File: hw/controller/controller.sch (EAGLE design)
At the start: 86 parts, among them J1 JST-PH3SMT_VERT, J2 JST-PH3SMT_VERT, Q1 TPN1R603PL, Q2 TPN1R603PL, Q3 TPN1R603PL, Q4 TPN1R603PL, Q5 TPN1R603PL, Q6 TPN1R603PL, U1 STM32F4R_64PIN, U2 DRV8323RS, U3 AS5147, U4 MAX13431E, U5 MAX13433EETD+T, X1 8.0MHz

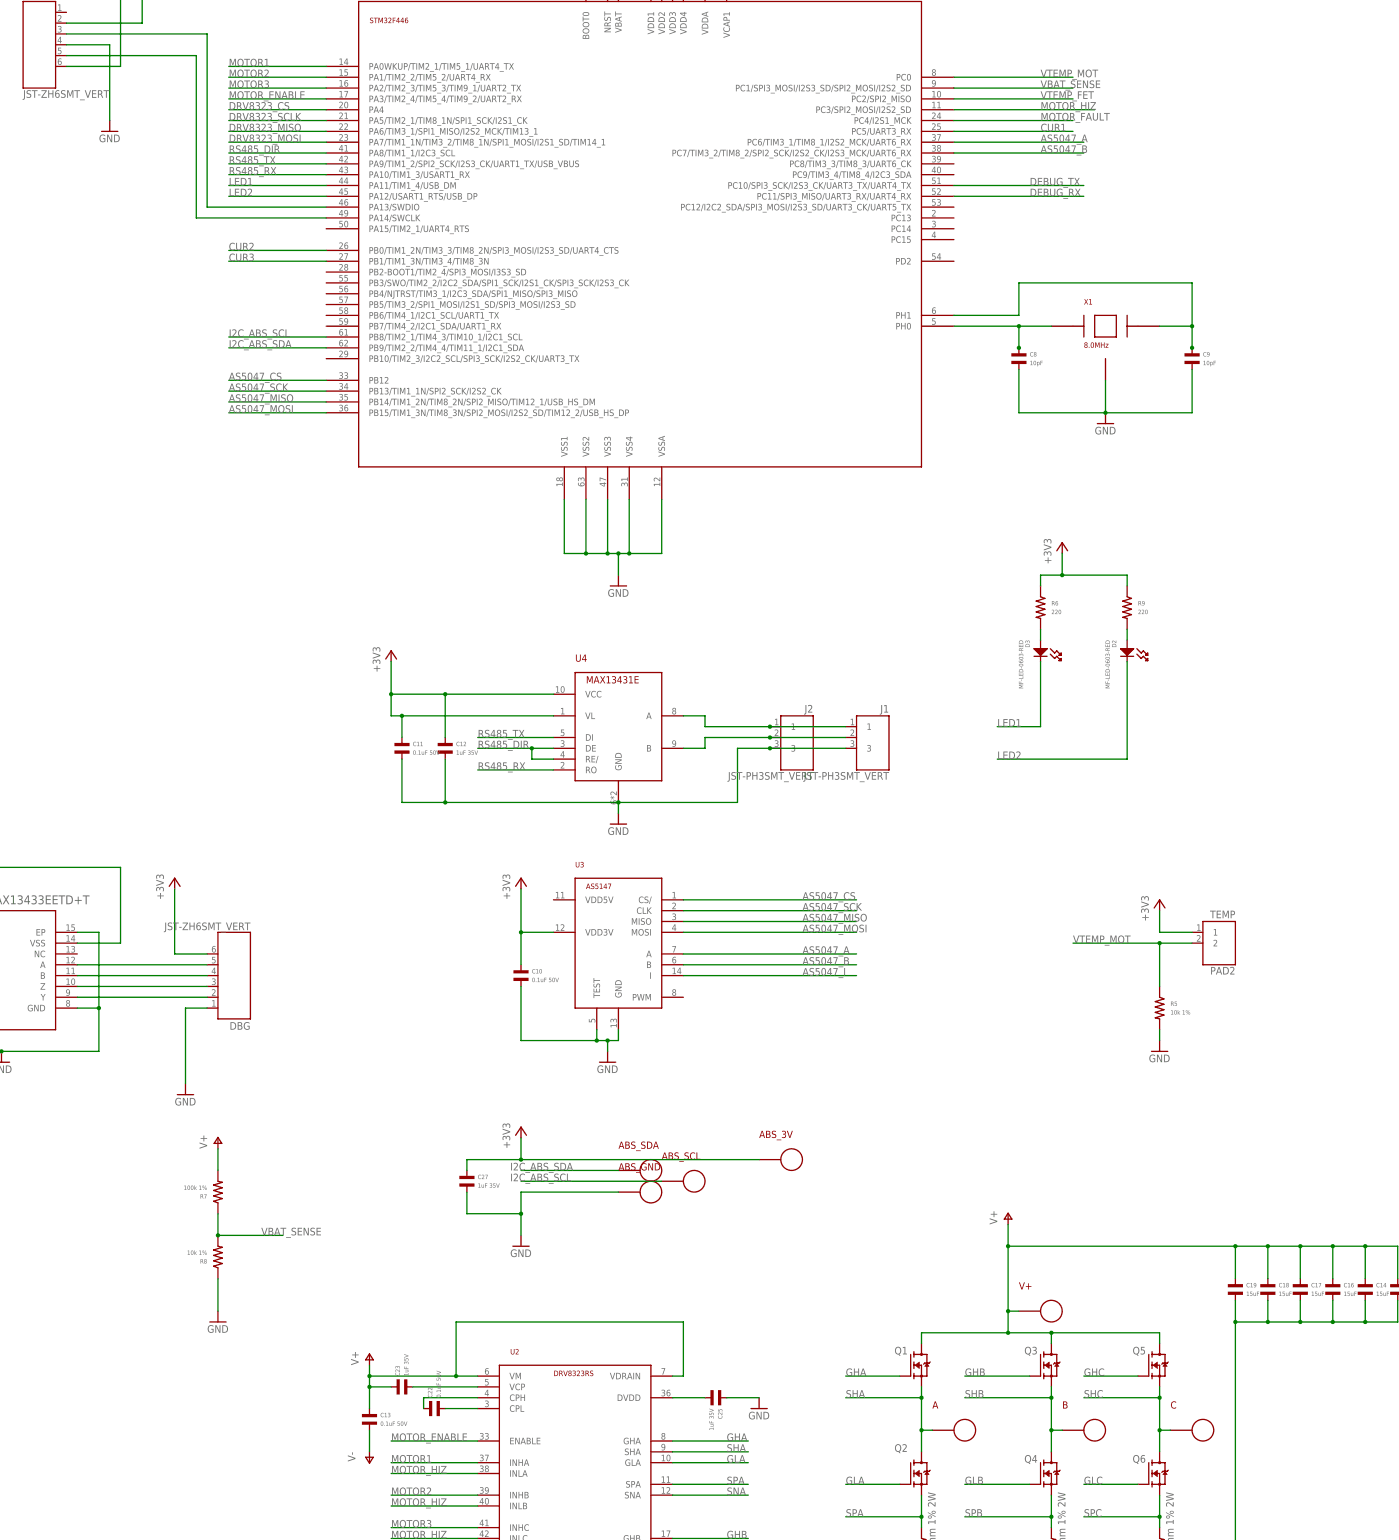
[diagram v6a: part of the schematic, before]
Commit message: Fix more errata in controller board
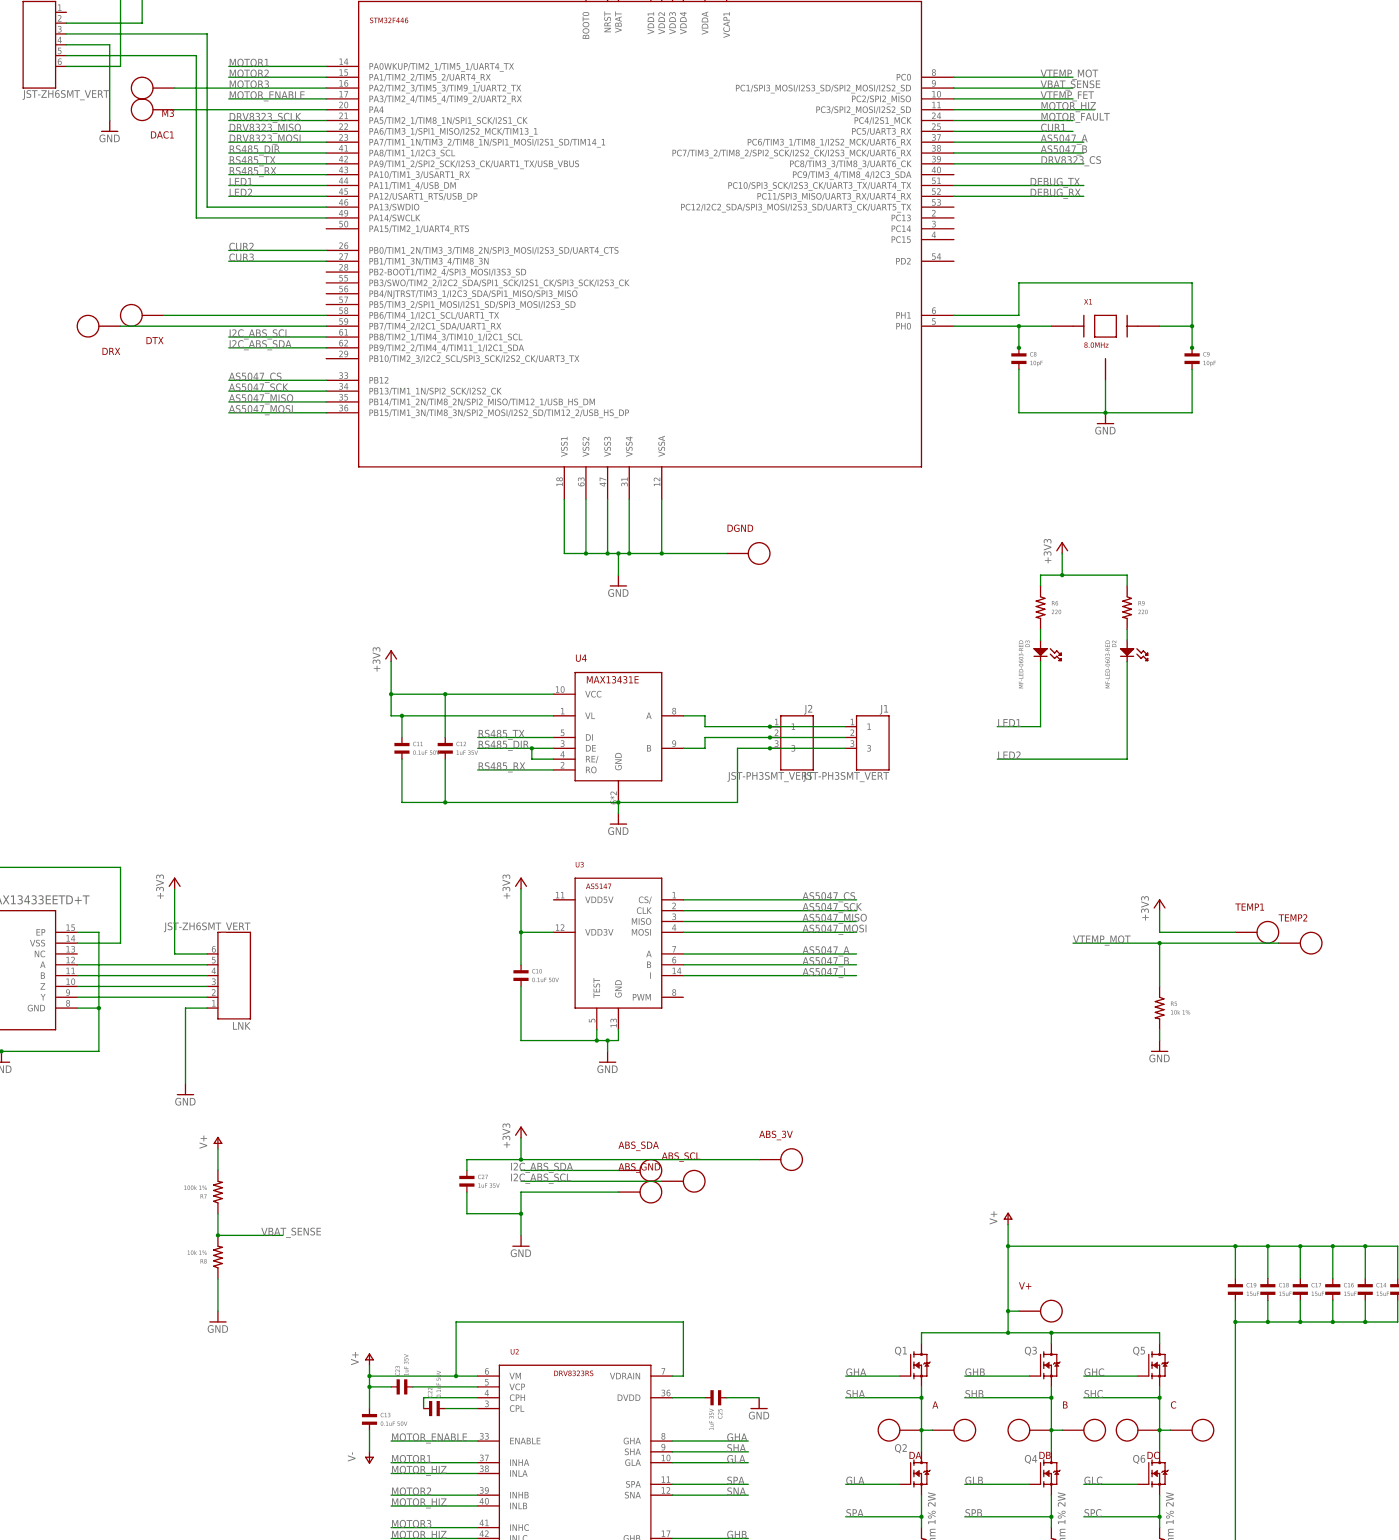
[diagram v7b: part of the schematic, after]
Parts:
- removed TEMP: PAD2, controller:PAD2
- added DA, DAC1, DB, DC, DGND, DRX, DTX, M3, TEMP1, TEMP2: PAD24AWG_PAD, controller:PAD24AWG_PAD
- R1: device mfpassives:RESISTOR_0402 -> mfpassives:RESISTOR_0603; MPN MF-RES-0402-220 -> MF-RES-0603-220
- renumbered DBG to LNK
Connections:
- new net N$1: DAC1.P$1, U1.PA4
- new net N$2: DTX.P$1, U1.PB6/TIM4_1/I2C1_SCL/UART1_TX
- new net N$3: DRX.P$1, U1.PB7/TIM4_2/I2C1_SDA/UART1_RX
- net +3V3: now also TEMP1.P$1; no longer TEMP.1
- net DRV8323_CS: now also U1.PC8/TIM3_3/TIM8_3/UART6_CK; no longer U1.PA4
- net GND: now also DGND.P$1
- net MOTOR3: now also M3.P$1
- net SHA: now also DA.P$1
- net SHB: now also DB.P$1
- net SHC: now also DC.P$1
- net VTEMP_MOT: now also TEMP2.P$1; no longer TEMP.2
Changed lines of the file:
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@@
 <part name="GND16" library="supply1" deviceset="GND" device=""/>
 <part name="+3V8" library="supply1" deviceset="+3V3" device=""/>
-<part name="R1" library="mfpassives" deviceset="RESISTOR" device="_0402" value="220">
+<part name="R1" library="mfpassives" deviceset="RESISTOR" device="_0603" value="220">
 <attribute name="HOUSEPART" value="1"/>
-<attribute name="MPN" value="MF-RES-0402-220"/>
+<attribute name="MPN" value="MF-RES-0603-220"/>
 </part>
 <part name="C2" library="mfpassives" deviceset="CAPACITOR_NP" device="_0402" value="0.1uF 50V">
@@
 <part name="GND10" library="supply1" deviceset="GND" device=""/>
 <part name="+3V5" library="supply1" deviceset="+3V3" device=""/>
-<part name="TEMP" library="controller" deviceset="PAD2" device="">
-<attribute name="POPULATE" value="0"/>
-</part>
 <part name="+3V6" library="supply1" deviceset="+3V3" device=""/>
 <part name="GND11" library="supply1" deviceset="GND" device=""/>
@@
 <part name="+3V11" library="supply1" deviceset="+3V3" device=""/>
 <part name="GND13" library="supply1" deviceset="GND" device=""/>
-<part name="DBG" library="controller" deviceset="JST-ZH6" device="SMT_VERT" value="JST-ZH6SMT_VERT">
+<part name="LNK" library="controller" deviceset="JST-ZH6" device="SMT_VERT" value="JST-ZH6SMT_VERT">
 <attribute name="MF" value="JST"/>
 <attribute name="MPN" value="B6B-ZR-SM4-TF(LF)(SN)"/>
@@
 <attribute name="MPN" value="C1005X7R1H104K050BE"/>
 </part>
+<part name="DAC1" library="controller" deviceset="PAD" device="24AWG_PAD"/>
+<part name="M3" library="controller" deviceset="PAD" device="24AWG_PAD"/>
+<part name="DTX" library="controller" deviceset="PAD" device="24AWG_PAD"/>
+<part name="DRX" library="controller" deviceset="PAD" device="24AWG_PAD"/>
+<part name="TEMP1" library="controller" deviceset="PAD" device="24AWG_PAD"/>
+<part name="TEMP2" library="controller" deviceset="PAD" device="24AWG_PAD"/>
+<part name="DGND" library="controller" deviceset="PAD" device="24AWG_PAD"/>
+<part name="DA" library="controller" deviceset="PAD" device="24AWG_PAD"/>
+<part name="DB" library="controller" deviceset="PAD" device="24AWG_PAD"/>
+<part name="DC" library="controller" deviceset="PAD" device="24AWG_PAD"/>
 </parts>
 <sheets>
@@
 <instance part="GND10" gate="1" x="66.04" y="-200.66"/>
 <instance part="+3V5" gate="G$1" x="66.04" y="-172.72"/>
-<instance part="TEMP" gate="A" x="228.6" y="-129.54" rot="MR0">
-<attribute name="POPULATE" x="228.6" y="-129.54" size="1.778" layer="96" rot="MR0" display="off"/>
-</instance>
 <instance part="+3V6" gate="G$1" x="215.9" y="-119.38"/>
 <instance part="GND11" gate="1" x="215.9" y="-154.94"/>
@@
 <instance part="+3V11" gate="G$1" x="-93.98" y="-104.14"/>
 <instance part="GND13" gate="1" x="-55.88" y="-157.48"/>
-<instance part="DBG" gate="A" x="-2.54" y="-137.16" rot="R180">
+<instance part="LNK" gate="A" x="-2.54" y="-137.16" rot="R180">
 <attribute name="POPULATE" x="-2.54" y="-137.16" size="1.778" layer="96" rot="R180" display="off"/>
 <attribute name="MPN" x="-2.54" y="-137.16" size="1.778" layer="96" rot="R180" display="off"/>
@@
 <attribute name="MF" x="228.6" y="-320.04" size="1.778" layer="96" display="off"/>
 </instance>
+<instance part="DAC1" gate="G$1" x="-22.86" y="66.04" rot="R180"/>
+<instance part="M3" gate="G$1" x="-22.86" y="71.12" rot="R180"/>
+<instance part="DTX" gate="G$1" x="-25.4" y="17.78" rot="R180"/>
+<instance part="DRX" gate="G$1" x="-35.56" y="15.24" rot="R180"/>
+<instance part="TEMP1" gate="G$1" x="241.3" y="-127"/>
+<instance part="TEMP2" gate="G$1" x="251.46" y="-129.54"/>
+<instance part="DGND" gate="G$1" x="121.92" y="-38.1"/>
+<instance part="DA" gate="G$1" x="152.4" y="-243.84" rot="R180"/>
+<instance part="DB" gate="G$1" x="182.88" y="-243.84" rot="R180"/>
+<instance part="DC" gate="G$1" x="208.28" y="-243.84" rot="R180"/>
 </instances>
 <busses>
@@
 <pinref part="+3V6" gate="G$1" pin="+3V3"/>
 <wire x1="215.9" y1="-121.92" x2="215.9" y2="-127" width="0.1524" layer="91"/>
-<pinref part="TEMP" gate="A" pin="1"/>
-<wire x1="215.9" y1="-127" x2="223.52" y2="-127" width="0.1524" layer="91"/>
+<pinref part="TEMP1" gate="G$1" pin="P$1"/>
+<wire x1="215.9" y1="-127" x2="233.68" y2="-127" width="0.1524" layer="91"/>
 </segment>
 <segment>
@@
 <pinref part="+3V10" gate="G$1" pin="+3V3"/>
 <wire x1="-15.24" y1="-116.84" x2="-15.24" y2="-132.08" width="0.1524" layer="91"/>
-<pinref part="DBG" gate="A" pin="6"/>
+<pinref part="LNK" gate="A" pin="6"/>
 <wire x1="-15.24" y1="-132.08" x2="-7.62" y2="-132.08" width="0.1524" layer="91"/>
 </segment>
@@
 <pinref part="U1" gate="G$1" pin="VSS4"/>
 <pinref part="U1" gate="G$1" pin="VSSA"/>
+<pinref part="DGND" gate="G$1" pin="P$1"/>
+<wire x1="99.06" y1="-38.1" x2="114.3" y2="-38.1" width="0.1524" layer="91"/>
+<junction x="99.06" y="-38.1"/>
 </segment>
 <segment>
@@
 <pinref part="GND3" gate="1" pin="GND"/>
 <wire x1="-12.7" y1="-162.56" x2="-12.7" y2="-144.78" width="0.1524" layer="91"/>
-<pinref part="DBG" gate="A" pin="1"/>
+<pinref part="LNK" gate="A" pin="1"/>
 <wire x1="-12.7" y1="-144.78" x2="-7.62" y2="-144.78" width="0.1524" layer="91"/>
 </segment>
@@
 <segment>
 <pinref part="U1" gate="G$1" pin="PA2/TIM2_3/TIM5_3/TIM9_1/UART2_TX"/>
-<wire x1="20.32" y1="71.12" x2="-2.54" y2="71.12" width="0.1524" layer="91"/>
+<wire x1="20.32" y1="71.12" x2="-15.24" y2="71.12" width="0.1524" layer="91"/>
 <label x="-2.54" y="71.12" size="1.778" layer="95"/>
+<pinref part="M3" gate="G$1" pin="P$1"/>
 </segment>
 </net>
@@
 </segment>
 <segment>
-<pinref part="U1" gate="G$1" pin="PA4"/>
-<wire x1="20.32" y1="66.04" x2="-2.54" y2="66.04" width="0.1524" layer="91"/>
-<label x="-2.54" y="66.04" size="1.778" layer="95"/>
+<pinref part="U1" gate="G$1" pin="PC8/TIM3_3/TIM8_3/UART6_CK"/>
+<wire x1="167.64" y1="53.34" x2="198.12" y2="53.34" width="0.1524" layer="91"/>
+<label x="187.96" y="53.34" size="1.778" layer="95"/>
 </segment>
 </net>
@@
 <wire x1="162.56" y1="-243.84" x2="160.02" y2="-243.84" width="0.1524" layer="91"/>
 <junction x="160.02" y="-243.84"/>
+<pinref part="DA" gate="G$1" pin="P$1"/>
 </segment>
 <segment>
@@
 <wire x1="193.04" y1="-243.84" x2="190.5" y2="-243.84" width="0.1524" layer="91"/>
 <junction x="190.5" y="-243.84"/>
+<pinref part="DB" gate="G$1" pin="P$1"/>
 </segment>
 <segment>
@@
 <wire x1="218.44" y1="-243.84" x2="215.9" y2="-243.84" width="0.1524" layer="91"/>
 <junction x="215.9" y="-243.84"/>
+<pinref part="DC" gate="G$1" pin="P$1"/>
 </segment>
 <segment>
@@
 <segment>
 <pinref part="U5" gate="A" pin="Y"/>
-<pinref part="DBG" gate="A" pin="2"/>
+<pinref part="LNK" gate="A" pin="2"/>
 <wire x1="-38.1" y1="-142.24" x2="-7.62" y2="-142.24" width="0.1524" layer="91"/>
 </segment>
@@
 <segment>
 <pinref part="U5" gate="A" pin="Z"/>
-<pinref part="DBG" gate="A" pin="3"/>
+<pinref part="LNK" gate="A" pin="3"/>
 <wire x1="-38.1" y1="-139.7" x2="-7.62" y2="-139.7" width="0.1524" layer="91"/>
 </segment>
@@
 <segment>
 <pinref part="U5" gate="A" pin="B"/>
-<pinref part="DBG" gate="A" pin="4"/>
+<pinref part="LNK" gate="A" pin="4"/>
 <wire x1="-38.1" y1="-137.16" x2="-7.62" y2="-137.16" width="0.1524" layer="91"/>
 </segment>
@@
 <segment>
 <pinref part="U5" gate="A" pin="A"/>
-<pinref part="DBG" gate="A" pin="5"/>
+<pinref part="LNK" gate="A" pin="5"/>
 <wire x1="-38.1" y1="-134.62" x2="-7.62" y2="-134.62" width="0.1524" layer="91"/>
 </segment>
@@
 <pinref part="R5" gate="G$1" pin="P$1"/>
 <wire x1="215.9" y1="-139.7" x2="215.9" y2="-129.54" width="0.1524" layer="91"/>
-<pinref part="TEMP" gate="A" pin="2"/>
-<wire x1="215.9" y1="-129.54" x2="223.52" y2="-129.54" width="0.1524" layer="91"/>
 <wire x1="215.9" y1="-129.54" x2="195.58" y2="-129.54" width="0.1524" layer="91"/>
 <junction x="215.9" y="-129.54"/>
 <label x="195.58" y="-129.54" size="1.778" layer="95"/>
+<pinref part="TEMP2" gate="G$1" pin="P$1"/>
+<wire x1="215.9" y1="-129.54" x2="243.84" y2="-129.54" width="0.1524" layer="91"/>
 </segment>
 <segment>
@@
 </segment>
 </net>
+<net name="N$1" class="0">
+<segment>
+<pinref part="DAC1" gate="G$1" pin="P$1"/>
+<pinref part="U1" gate="G$1" pin="PA4"/>
+<wire x1="-15.24" y1="66.04" x2="20.32" y2="66.04" width="0.1524" layer="91"/>
+</segment>
+</net>
+<net name="N$2" class="0">
+<segment>
+<pinref part="DTX" gate="G$1" pin="P$1"/>
+<pinref part="U1" gate="G$1" pin="PB6/TIM4_1/I2C1_SCL/UART1_TX"/>
+<wire x1="-17.78" y1="17.78" x2="20.32" y2="17.78" width="0.1524" layer="91"/>
+</segment>
+</net>
+<net name="N$3" class="0">
+<segment>
+<pinref part="DRX" gate="G$1" pin="P$1"/>
+<pinref part="U1" gate="G$1" pin="PB7/TIM4_2/I2C1_SDA/UART1_RX"/>
+<wire x1="-27.94" y1="15.24" x2="20.32" y2="15.24" width="0.1524" layer="91"/>
+</segment>
+</net>

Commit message: More tweaks to controller board
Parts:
- removed R10, R3: 100k 1%, mfpassives:RESISTOR_0402
- R11: value 100k 1% -> 33k 1%; MPN ERJ-2RKF1003X -> ERJ-2RKF3302X
- U5: MF (none) -> Maxim; MPN (none) -> MAX13433EETD+T; POPULATE (none) -> 1
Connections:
- net +3V3: no longer R10.P$1, R3.P$1
- net N$8: no longer R10.P$2, R3.P$2
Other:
- note removed: "3x 100k = 33.3k (to save part count)"
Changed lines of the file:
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@@
 <attribute name="MPN" value="C3216X5R1V156M160AC"/>
 </part>
-<part name="R3" library="mfpassives" deviceset="RESISTOR" device="_0402" value="100k 1%">
+<part name="R11" library="mfpassives" deviceset="RESISTOR" device="_0402" value="33k 1%">
 <attribute name="MF" value="Panasonic"/>
-<attribute name="MPN" value="ERJ-2RKF1003X"/>
-</part>
-<part name="R10" library="mfpassives" deviceset="RESISTOR" device="_0402" value="100k 1%">
-<attribute name="MF" value="Panasonic"/>
-<attribute name="MPN" value="ERJ-2RKF1003X"/>
-</part>
-<part name="R11" library="mfpassives" deviceset="RESISTOR" device="_0402" value="100k 1%">
-<attribute name="MF" value="Panasonic"/>
-<attribute name="MPN" value="ERJ-2RKF1003X"/>
+<attribute name="MPN" value="ERJ-2RKF3302X"/>
 </part>
 <part name="C29" library="mfpassives" deviceset="CAPACITOR_NP" device="_0402" value="1uF 35V">
@@
 <part name="ABS_SCL" library="controller" deviceset="PAD" device="24AWG_PAD"/>
 <part name="ABS_GND" library="controller" deviceset="PAD" device="24AWG_PAD"/>
-<part name="U5" library="controller" deviceset="MAX13433EETD+T" device=""/>
+<part name="U5" library="controller" deviceset="MAX13433EETD+T" device="">
+<attribute name="MF" value="Maxim"/>
+<attribute name="MPN" value="MAX13433EETD+T"/>
+<attribute name="POPULATE" value="1"/>
+</part>
 <part name="+3V11" library="supply1" deviceset="+3V3" device=""/>
 <part name="GND13" library="supply1" deviceset="GND" device=""/>
@@
 <sheet>
 <plain>
-<text x="145.034" y="-324.358" size="1.778" layer="91">3x 100k = 33.3k
-(to save part count)</text>
 </plain>
 <instances>
@@
 <attribute name="MF" x="233.68" y="-210.82" size="1.778" layer="96" display="off"/>
 </instance>
-<instance part="R3" gate="G$1" x="152.4" y="-330.2">
-<attribute name="MPN" x="152.4" y="-330.2" size="1.778" layer="96" display="off"/>
-<attribute name="MF" x="152.4" y="-330.2" size="1.778" layer="96" display="off"/>
-</instance>
-<instance part="R10" gate="G$1" x="144.78" y="-330.2">
-<attribute name="MPN" x="144.78" y="-330.2" size="1.778" layer="96" display="off"/>
-<attribute name="MF" x="144.78" y="-330.2" size="1.778" layer="96" display="off"/>
-</instance>
 <instance part="R11" gate="G$1" x="134.62" y="-330.2">
 <attribute name="MPN" x="134.62" y="-330.2" size="1.778" layer="96" display="off"/>
@@
 <instance part="ABS_SCL" gate="G$1" x="106.68" y="-185.42"/>
 <instance part="ABS_GND" gate="G$1" x="96.52" y="-187.96"/>
-<instance part="U5" gate="A" x="-76.2" y="-127"/>
+<instance part="U5" gate="A" x="-76.2" y="-127">
+<attribute name="MPN" x="-76.2" y="-127" size="1.778" layer="96" display="off"/>
+<attribute name="MF" x="-76.2" y="-127" size="1.778" layer="96" display="off"/>
+<attribute name="POPULATE" x="-76.2" y="-127" size="1.778" layer="96" display="off"/>
+</instance>
 <instance part="+3V11" gate="G$1" x="-93.98" y="-104.14"/>
 <instance part="GND13" gate="1" x="-55.88" y="-157.48"/>
@@
 <pinref part="R11" gate="G$1" pin="P$1"/>
 <junction x="134.62" y="-325.12"/>
-<pinref part="R10" gate="G$1" pin="P$1"/>
-<wire x1="134.62" y1="-325.12" x2="144.78" y2="-325.12" width="0.1524" layer="91"/>
-<pinref part="R3" gate="G$1" pin="P$1"/>
-<wire x1="144.78" y1="-325.12" x2="152.4" y2="-325.12" width="0.1524" layer="91"/>
-<junction x="144.78" y="-325.12"/>
 </segment>
 <segment>
@@
 <junction x="134.62" y="-337.82"/>
 <pinref part="R11" gate="G$1" pin="P$2"/>
-<pinref part="R10" gate="G$1" pin="P$2"/>
-<wire x1="134.62" y1="-337.82" x2="144.78" y2="-337.82" width="0.1524" layer="91"/>
-<wire x1="144.78" y1="-337.82" x2="144.78" y2="-335.28" width="0.1524" layer="91"/>
-<pinref part="R3" gate="G$1" pin="P$2"/>
-<wire x1="144.78" y1="-337.82" x2="152.4" y2="-337.82" width="0.1524" layer="91"/>
-<wire x1="152.4" y1="-337.82" x2="152.4" y2="-335.28" width="0.1524" layer="91"/>
-<junction x="144.78" y="-337.82"/>
-</segment>
-</net>
+</segment>
+</net>
